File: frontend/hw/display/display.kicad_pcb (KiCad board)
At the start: 2 copper layers, 43.9 x 44.5 mm, 15 parts, among them J1 Conn_01x04, J2 Conn_02x17_Odd_Even, Q1 MMBT3904, Q2 MMBT3904, U1 ESP32-WROOM-32U, U2 CH340C, U3 AMS1117-3.3

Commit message: Add boot switch.
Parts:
- removed R5, R6: 10K, Resistor_SMD:R_0603_1608Metric
- added R1: 10K, Resistor_SMD:R_0603_1608Metric, F.Cu at (95.0, 96.8)
- added R2: 10K, Resistor_SMD:R_0603_1608Metric, F.Cu at (95.0, 89.2)
- added SW1: SW_Push, Button_Switch_SMD:SW_Push_SPST_NO_Alps_SKRK, F.Cu at (97.9, 83.8)
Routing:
- net IO0: track 23.1 -> 28.3 mm
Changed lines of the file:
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@@
   (net 61 "unconnected-(U2-Pad12)")
   (net 62 "unconnected-(U2-Pad15)")
+  (footprint "Button_Switch_SMD:SW_Push_SPST_NO_Alps_SKRK" (layer "F.Cu")
+    (at 97.917 83.82 180)
+    (descr "http://www.alps.com/prod/info/E/HTML/Tact/SurfaceMount/SKRK/SKRKAHE020.html")
+    (tags "SMD SMT button")
+    (property "Sheetfile" "display.kicad_sch")
+    (property "Sheetname" "")
+    (attr smd)
+    (fp_text reference "SW1" (at -2.794 -2.921) (layer "F.SilkS")
+      (effects (font (size 1 1) (thickness 0.15)))
+    )
+    (fp_text value "SW_Push" (at 0 2.5) (layer "F.Fab")
+      (effects (font (size 1 1) (thickness 0.15)))
+    )
+    (fp_text user "${REFERENCE}" (at 0 0) (layer "F.Fab")
+      (effects (font (size 1 1) (thickness 0.15)))
+    )
+    (fp_line (start -2.07 -1.57) (end 2.07 -1.57) (layer "F.SilkS") (width 0.12))
+    (fp_line (start 2.07 1.57) (end -2.07 1.57) (layer "F.SilkS") (width 0.12))
+    (fp_line (start 2.07 1.27) (end 2.07 1.57) (layer "F.SilkS") (width 0.12))
+    (fp_line (start 2.07 -1.57) (end 2.07 -1.27) (layer "F.SilkS") (width 0.12))
+    (fp_line (start -2.07 1.57) (end -2.07 1.27) (layer "F.SilkS") (width 0.12))
+    (fp_line (start -2.07 -1.27) (end -2.07 -1.57) (layer "F.SilkS") (width 0.12))
+    (fp_line (start -2.75 1.7) (end -2.75 -1.7) (layer "F.CrtYd") (width 0.05))
+    (fp_line (start 2.75 1.7) (end -2.75 1.7) (layer "F.CrtYd") (width 0.05))
+    (fp_line (start 2.75 -1.7) (end 2.75 1.7) (layer "F.CrtYd") (width 0.05))
+    (fp_line (start -2.75 -1.7) (end 2.75 -1.7) (layer "F.CrtYd") (width 0.05))
+    (fp_line (start 1.95 1.45) (end -1.95 1.45) (layer "F.Fab") (width 0.1))
+    (fp_line (start -1.95 1.45) (end -1.95 -1.45) (layer "F.Fab") (width 0.1))
+    (fp_line (start 1.95 -1.45) (end 1.95 1.45) (layer "F.Fab") (width 0.1))
+    (fp_line (start -1.95 -1.45) (end 1.95 -1.45) (layer "F.Fab") (width 0.1))
+    (fp_circle (center 0 0) (end 1 0) (layer "F.Fab") (width 0.1) (fill none))
+    (pad "1" smd roundrect (at -2.1 0 180) (size 0.8 2) (layers "F.Cu" "F.Paste" "F.Mask") (roundrect_rratio 0.25)
+      (net 2 "GND") (pinfunction "1") (pintype "passive"))
+    (pad "2" smd roundrect (at 2.1 0 180) (size 0.8 2) (layers "F.Cu" "F.Paste" "F.Mask") (roundrect_rratio 0.25)
+      (net 32 "IO0") (pinfunction "2") (pintype "passive"))
+    (model "${KICAD6_3DMODEL_DIR}/Button_Switch_SMD.3dshapes/SW_Push_SPST_NO_Alps_SKRK.wrl"
+      (offset (xyz 0 0 0))
+      (scale (xyz 1 1 1))
+      (rotate (xyz 0 0 0))
+    )
+  )
   (footprint "Package_TO_SOT_SMD:SOT-223-3_TabPin2" (layer "F.Cu")
     (at 88.392 72.39)
@@
     )
   )
+  (footprint "Resistor_SMD:R_0603_1608Metric" (layer "F.Cu")
+    (at 94.996 89.154 90)
+    (descr "Resistor SMD 0603 (1608 Metric), square (rectangular) end terminal, IPC_7351 nominal, (Body size source: http://www.tortai-tech.com/upload/download/2011102023233369053.pdf), generated with kicad-footprint-generator")
+    (tags "resistor")
+    (property "Sheetfile" "display.kicad_sch")
+    (property "Sheetname" "")
+    (attr smd)
+    (fp_text reference "R2" (at 0 1.651 90) (layer "F.SilkS")
+      (effects (font (size 1 1) (thickness 0.15)))
+    )
+    (fp_text value "10K" (at 0 1.43 90) (layer "F.Fab")
+      (effects (font (size 1 1) (thickness 0.15)))
+    )
+    (fp_text user "${REFERENCE}" (at 0 0 90) (layer "F.Fab")
+      (effects (font (size 0.4 0.4) (thickness 0.06)))
+    )
+    (fp_line (start -0.162779 -0.51) (end 0.162779 -0.51) (layer "F.SilkS") (width 0.12))
+    (fp_line (start -0.162779 0.51) (end 0.162779 0.51) (layer "F.SilkS") (width 0.12))
+    (fp_line (start 1.48 0.73) (end -1.48 0.73) (layer "F.CrtYd") (width 0.05))
+    (fp_line (start -1.48 -0.73) (end 1.48 -0.73) (layer "F.CrtYd") (width 0.05))
+    (fp_line (start -1.48 0.73) (end -1.48 -0.73) (layer "F.CrtYd") (width 0.05))
+    (fp_line (start 1.48 -0.73) (end 1.48 0.73) (layer "F.CrtYd") (width 0.05))
+    (fp_line (start 0.8 0.4) (end -0.8 0.4) (layer "F.Fab") (width 0.1))
+    (fp_line (start 0.8 -0.4) (end 0.8 0.4) (layer "F.Fab") (width 0.1))
+    (fp_line (start -0.8 -0.4) (end 0.8 -0.4) (layer "F.Fab") (width 0.1))
+    (fp_line (start -0.8 0.4) (end -0.8 -0.4) (layer "F.Fab") (width 0.1))
+    (pad "1" smd roundrect locked (at -0.7875 0 90) (size 0.875 0.95) (layers "F.Cu" "F.Paste" "F.Mask") (roundrect_rratio 0.25)
+      (net 28 "Net-(Q1-Pad2)") (pintype "passive"))
+    (pad "2" smd roundrect locked (at 0.7875 0 90) (size 0.875 0.95) (layers "F.Cu" "F.Paste" "F.Mask") (roundrect_rratio 0.25)
+      (net 30 "Net-(Q2-Pad1)") (pintype "passive"))
+    (model "${KICAD6_3DMODEL_DIR}/Resistor_SMD.3dshapes/R_0603_1608Metric.wrl"
+      (offset (xyz 0 0 0))
+      (scale (xyz 1 1 1))
+      (rotate (xyz 0 0 0))
+    )
+  )
   (footprint "Capacitor_SMD:C_0805_2012Metric" (layer "F.Cu")
     (at 91.44 97.028 -90)
@@
       (net 32 "IO0") (pinfunction "C") (pintype "passive"))
     (model "${KICAD6_3DMODEL_DIR}/Package_TO_SOT_SMD.3dshapes/SOT-23.wrl"
-      (offset (xyz 0 0 0))
-      (scale (xyz 1 1 1))
-      (rotate (xyz 0 0 0))
-    )
-  )
-  (footprint "Resistor_SMD:R_0603_1608Metric" (layer "F.Cu")
-    (at 94.996 89.154 90)
-    (descr "Resistor SMD 0603 (1608 Metric), square (rectangular) end terminal, IPC_7351 nominal, (Body size source: http://www.tortai-tech.com/upload/download/2011102023233369053.pdf), generated with kicad-footprint-generator")
-    (tags "resistor")
-    (property "Sheetfile" "display.kicad_sch")
-    (property "Sheetname" "")
-    (attr smd)
-    (fp_text reference "R6" (at 0 1.27 90) (layer "F.SilkS")
-      (effects (font (size 1 1) (thickness 0.15)))
-    )
-    (fp_text value "10K" (at 0 1.43 90) (layer "F.Fab")
-      (effects (font (size 1 1) (thickness 0.15)))
-    )
-    (fp_text user "${REFERENCE}" (at 0 0 90) (layer "F.Fab")
-      (effects (font (size 0.4 0.4) (thickness 0.06)))
-    )
-    (fp_line (start -0.162779 -0.51) (end 0.162779 -0.51) (layer "F.SilkS") (width 0.12))
-    (fp_line (start -0.162779 0.51) (end 0.162779 0.51) (layer "F.SilkS") (width 0.12))
-    (fp_line (start 1.48 -0.73) (end 1.48 0.73) (layer "F.CrtYd") (width 0.05))
-    (fp_line (start -1.48 -0.73) (end 1.48 -0.73) (layer "F.CrtYd") (width 0.05))
-    (fp_line (start 1.48 0.73) (end -1.48 0.73) (layer "F.CrtYd") (width 0.05))
-    (fp_line (start -1.48 0.73) (end -1.48 -0.73) (layer "F.CrtYd") (width 0.05))
-    (fp_line (start 0.8 0.4) (end -0.8 0.4) (layer "F.Fab") (width 0.1))
-    (fp_line (start 0.8 -0.4) (end 0.8 0.4) (layer "F.Fab") (width 0.1))
-    (fp_line (start -0.8 -0.4) (end 0.8 -0.4) (layer "F.Fab") (width 0.1))
-    (fp_line (start -0.8 0.4) (end -0.8 -0.4) (layer "F.Fab") (width 0.1))
-    (pad "1" smd roundrect locked (at -0.7875 0 90) (size 0.875 0.95) (layers "F.Cu" "F.Paste" "F.Mask") (roundrect_rratio 0.25)
-      (net 28 "Net-(Q1-Pad2)") (pintype "passive"))
-    (pad "2" smd roundrect locked (at 0.7875 0 90) (size 0.875 0.95) (layers "F.Cu" "F.Paste" "F.Mask") (roundrect_rratio 0.25)
-      (net 30 "Net-(Q2-Pad1)") (pintype "passive"))
-    (model "${KICAD6_3DMODEL_DIR}/Resistor_SMD.3dshapes/R_0603_1608Metric.wrl"
       (offset (xyz 0 0 0))
       (scale (xyz 1 1 1))
@@
     (property "Sheetname" "")
     (attr smd)
-    (fp_text reference "R5" (at 0 1.524 90) (layer "F.SilkS")
+    (fp_text reference "R1" (at 0.254 1.524 90) (layer "F.SilkS")
       (effects (font (size 1 1) (thickness 0.15)))
     )
@@
     (fp_line (start -0.162779 -0.51) (end 0.162779 -0.51) (layer "F.SilkS") (width 0.12))
     (fp_line (start -0.162779 0.51) (end 0.162779 0.51) (layer "F.SilkS") (width 0.12))
+    (fp_line (start -1.48 0.73) (end -1.48 -0.73) (layer "F.CrtYd") (width 0.05))
+    (fp_line (start 1.48 -0.73) (end 1.48 0.73) (layer "F.CrtYd") (width 0.05))
+    (fp_line (start 1.48 0.73) (end -1.48 0.73) (layer "F.CrtYd") (width 0.05))
     (fp_line (start -1.48 -0.73) (end 1.48 -0.73) (layer "F.CrtYd") (width 0.05))
-    (fp_line (start 1.48 0.73) (end -1.48 0.73) (layer "F.CrtYd") (width 0.05))
-    (fp_line (start 1.48 -0.73) (end 1.48 0.73) (layer "F.CrtYd") (width 0.05))
-    (fp_line (start -1.48 0.73) (end -1.48 -0.73) (layer "F.CrtYd") (width 0.05))
+    (fp_line (start -0.8 0.4) (end -0.8 -0.4) (layer "F.Fab") (width 0.1))
+    (fp_line (start -0.8 -0.4) (end 0.8 -0.4) (layer "F.Fab") (width 0.1))
     (fp_line (start 0.8 -0.4) (end 0.8 0.4) (layer "F.Fab") (width 0.1))
-    (fp_line (start -0.8 -0.4) (end 0.8 -0.4) (layer "F.Fab") (width 0.1))
-    (fp_line (start -0.8 0.4) (end -0.8 -0.4) (layer "F.Fab") (width 0.1))
     (fp_line (start 0.8 0.4) (end -0.8 0.4) (layer "F.Fab") (width 0.1))
     (pad "1" smd roundrect locked (at -0.7875 0 90) (size 0.875 0.95) (layers "F.Cu" "F.Paste" "F.Mask") (roundrect_rratio 0.25)
@@
   (segment (start 71.764 81.491) (end 72.088511 81.815511) (width 0.25) (layer "F.Cu") (net 32))
   (segment (start 72.088511 81.815511) (end 78.767511 81.815511) (width 0.25) (layer "F.Cu") (net 32))
+  (segment (start 92.71 83.82) (end 91.186 85.344) (width 0.25) (layer "F.Cu") (net 32))
+  (segment (start 95.817 83.82) (end 92.71 83.82) (width 0.25) (layer "F.Cu") (net 32))
   (segment (start 91.186 85.344) (end 91.186 87.36) (width 0.25) (layer "F.Cu") (net 32))
   (segment (start 91.186 87.36) (end 91.202 87.376) (width 0.25) (layer "F.Cu") (net 32))

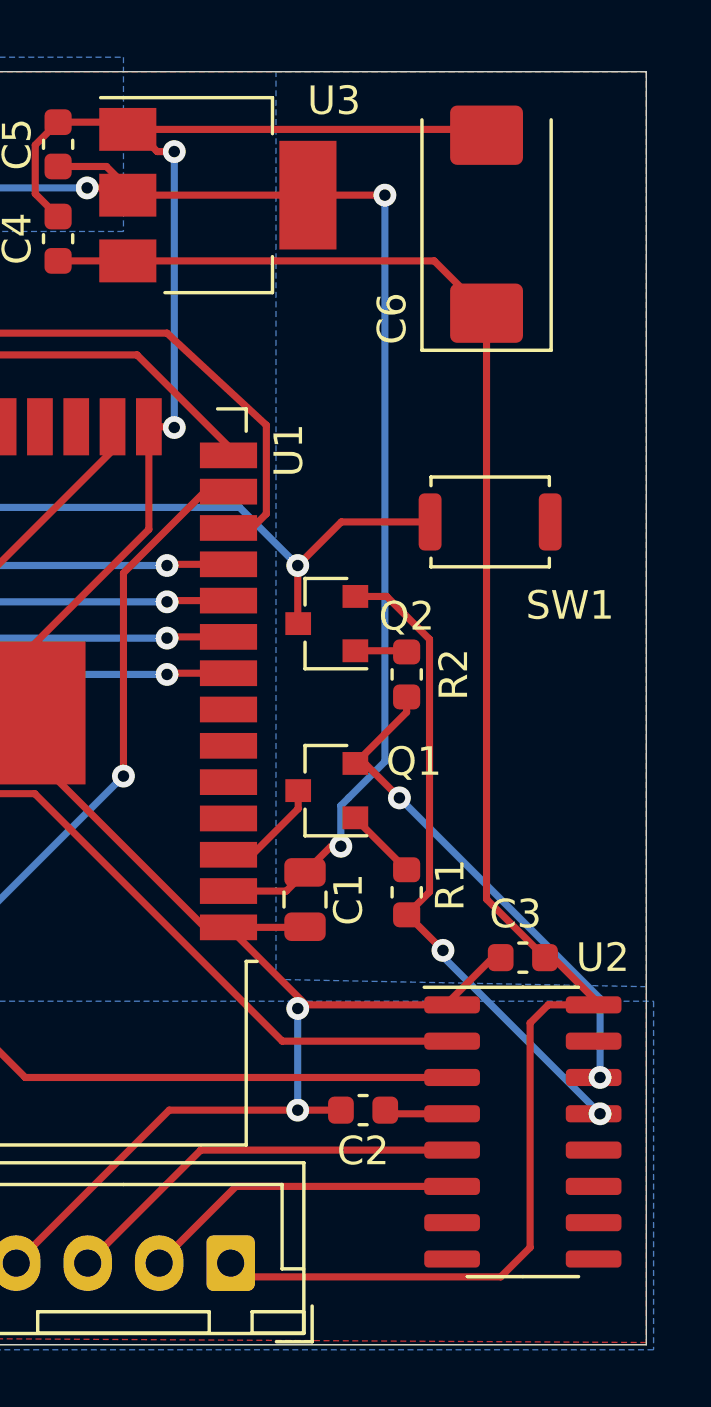
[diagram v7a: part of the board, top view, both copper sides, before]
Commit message: Add buttons.
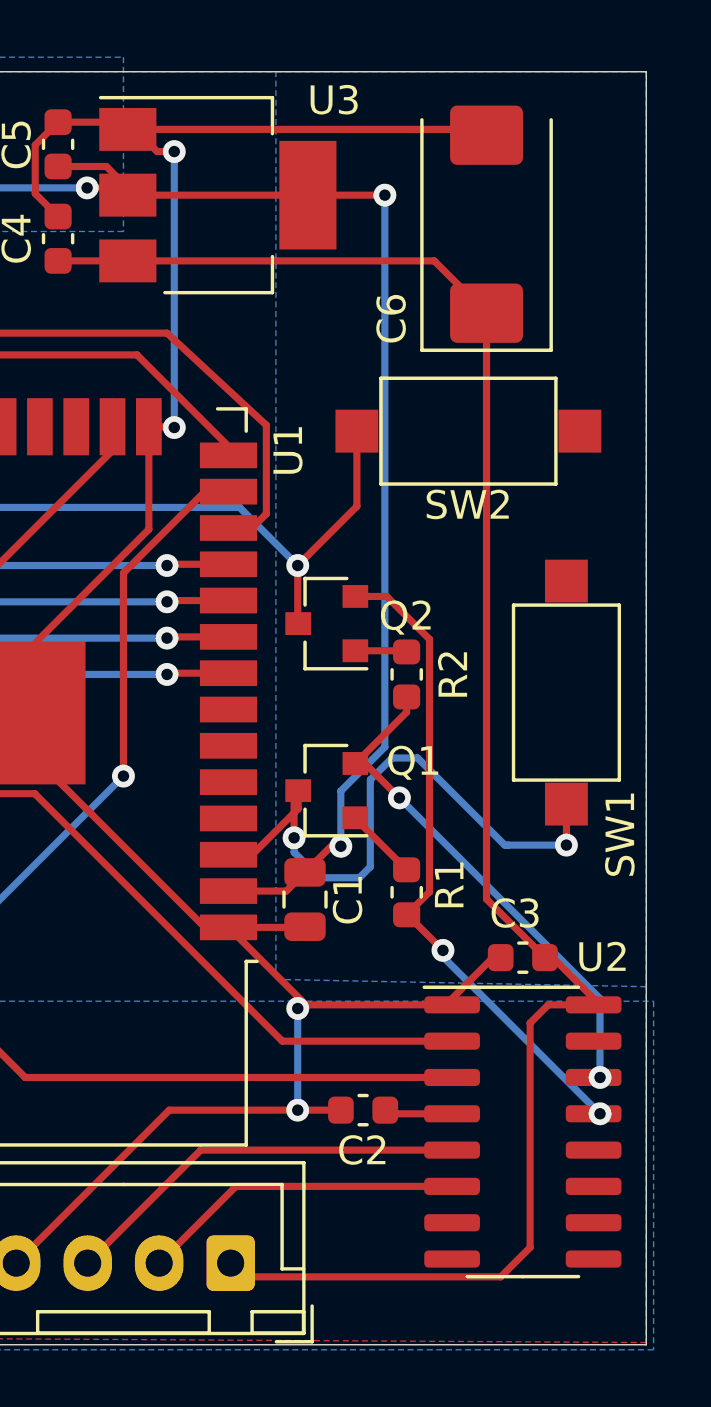
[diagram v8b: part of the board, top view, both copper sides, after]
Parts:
- added SW2: SW_SPST, Button_Switch_SMD:SW_SPST_CK_RS282G05A3, F.Cu at (97.2, 80.6)
- SW1: value SW_Push -> SW_SPST; footprint Button_Switch_SMD:SW_Push_SPST_NO_Alps_SKRK -> Button_Switch_SMD:SW_SPST_CK_RS282G05A3
- moved SW1 6.54 mm to (100.6, 89.8), turned to -90 degrees
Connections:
- SW1 pad 2: IO0 -> EN
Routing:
- net EN: track 3.74 -> 22.1 mm, vias 0 -> 2
